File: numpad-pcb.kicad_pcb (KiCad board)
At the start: 2 copper layers, 76.2 x 118.8 mm, 62 parts, among them J1 AVR-ISP-6, SW1 SW_Push, SW10 7/home, SW11 4/left, SW12 8/up, SW13 5, SW14 9/pgup, SW15 6/right, SW16 +, SW18 1/end, SW19 0/insert, SW2 ESC, SW20 2/down, SW22 3/pgdn, SW23 ./delete, SW24 ENTER, SW3 TAB, SW4 BACKSPACE, SW5 FN, SW6 NUM_LOCK, SW7 /, SW8 *, SW9 -, U1 ATmega32U4-A, Y1 Crystal_GND24_Small

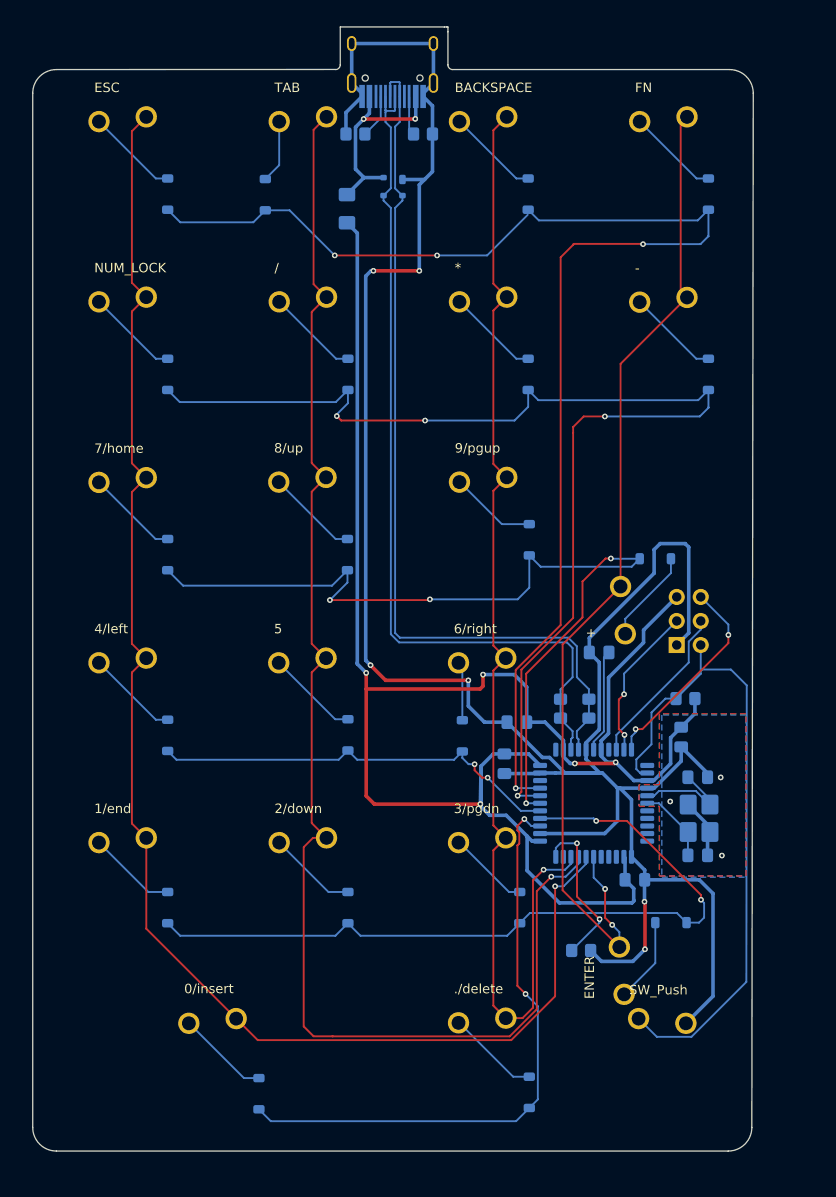
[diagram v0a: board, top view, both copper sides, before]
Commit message: Add copper ground pour
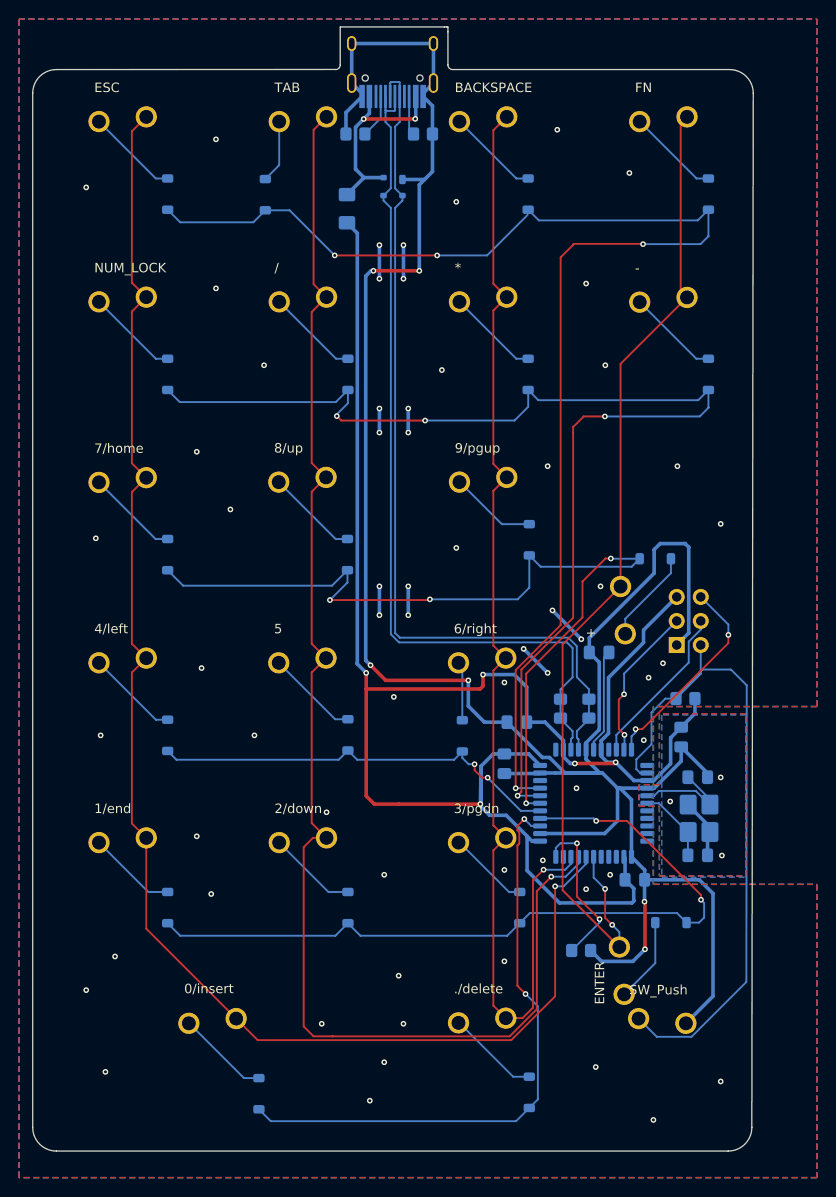
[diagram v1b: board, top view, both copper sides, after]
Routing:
- net GND: track 260.7 -> 286.9 mm, vias 9 -> 68
- net (no net): vias 0 -> 4

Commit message: Add USB-C shield protection
Changed the USB-C shield from being connected to ground to being
connected to a ferrite bead low pass filter to manage ESD. Also adjusted
ground around USB to prevent ESD from damaging nearby components.
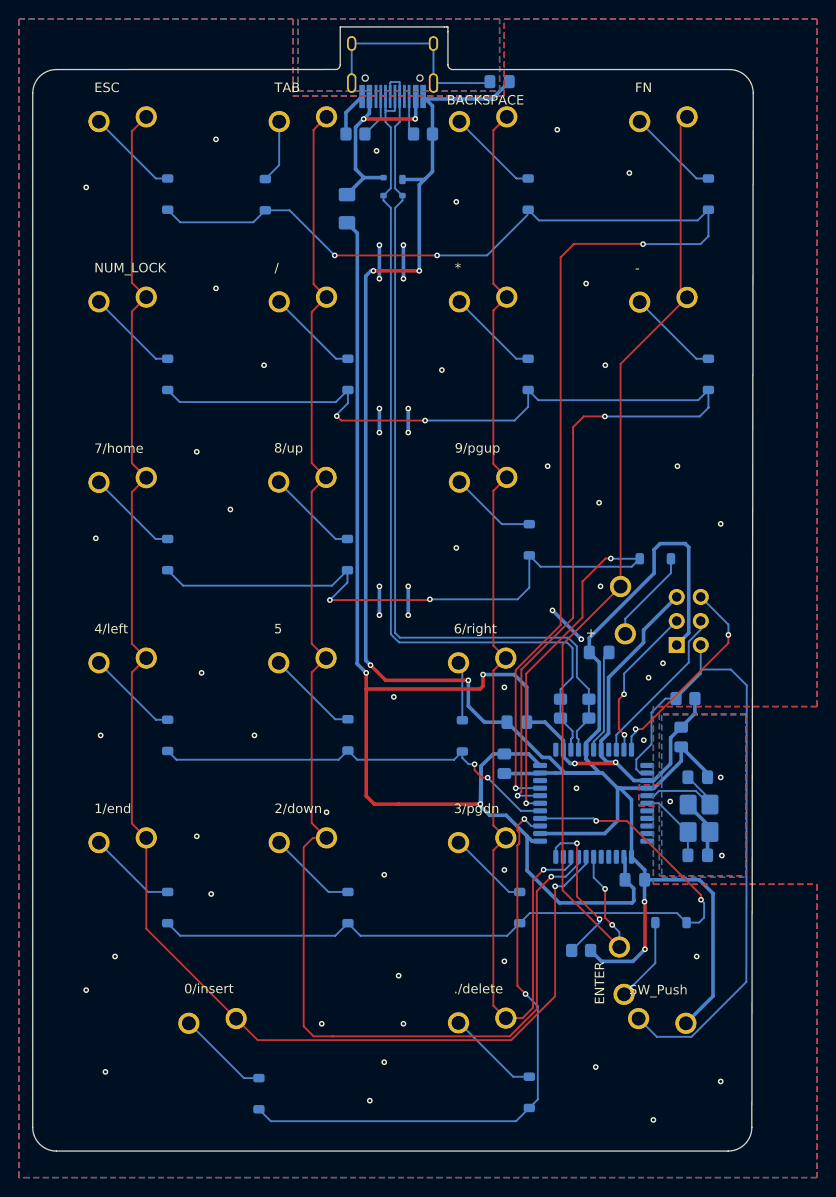
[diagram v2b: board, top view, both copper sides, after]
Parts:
- added FB1: 60@100MHz, Inductor_SMD:L_0805_2012Metric_Pad1.15x1.40mm_HandSolder, B.Cu at (99.1, 46.7)
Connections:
- USB1 pad 13: GND -> Earth
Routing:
- net Earth: track 0.00 -> 23.0 mm
- net GND: track 286.9 -> 272.8 mm, vias 68 -> 67
- net (no net): vias 4 -> 3
